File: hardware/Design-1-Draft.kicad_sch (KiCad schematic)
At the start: 37 parts, among them J1 Barrel_Jack_Switch, M1 WATERPUMP-1, M2 WATERPUMP-2, Q1 IRLZ44N, Q2 IRLZ44N, Q3 PN2222A, SW1 Button, U3 ADS1115, U5 Tang_Nano_9K, U7 BOB-12009

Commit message: Updated PCB & SCHEM
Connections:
- net AGND is gone; now on net GND: C7.2
- net GND: now also C8.1, U4.4 (OUT-); no longer C8.2, J1.2
- net at A1.30 (VIN), BZ1.1 (+), C1.1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: now also C8.2, U4.3 (OUT+); no longer C8.1, D1.1 (K)
- net at U4.1 (IN+): now also D1.1 (K)
- net at U4.2 (IN-): now also J1.2
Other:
- moved on the sheet: C8, U4

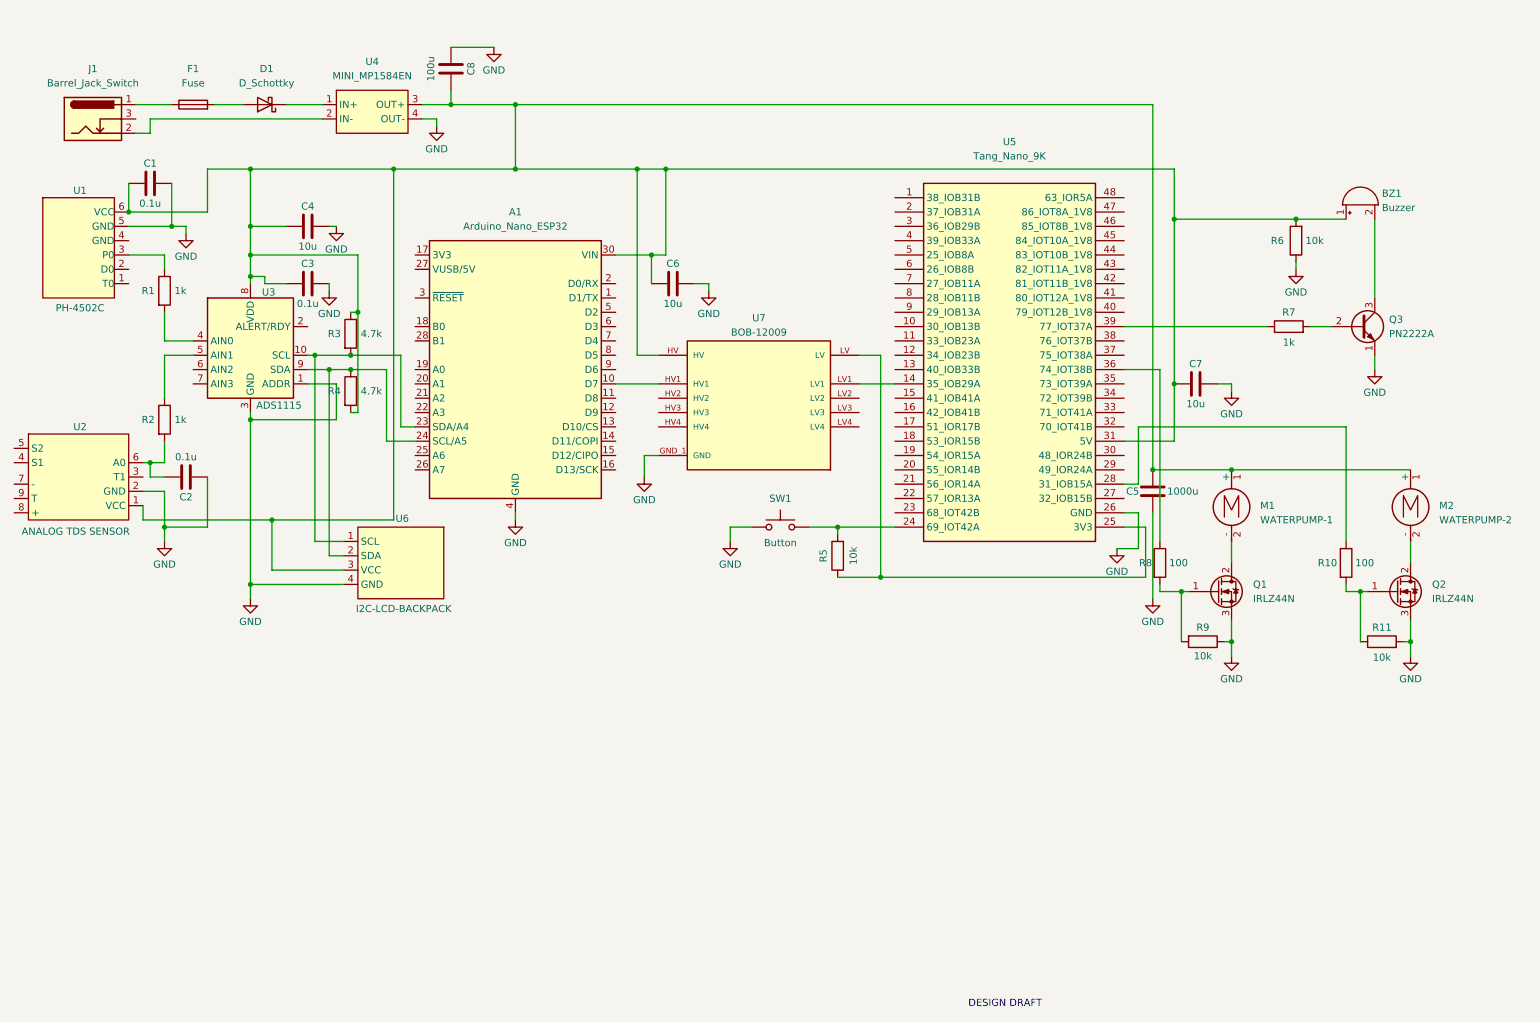
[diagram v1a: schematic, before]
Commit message: updated schem (added multiple caps & 2 flyback diodes @pumps)
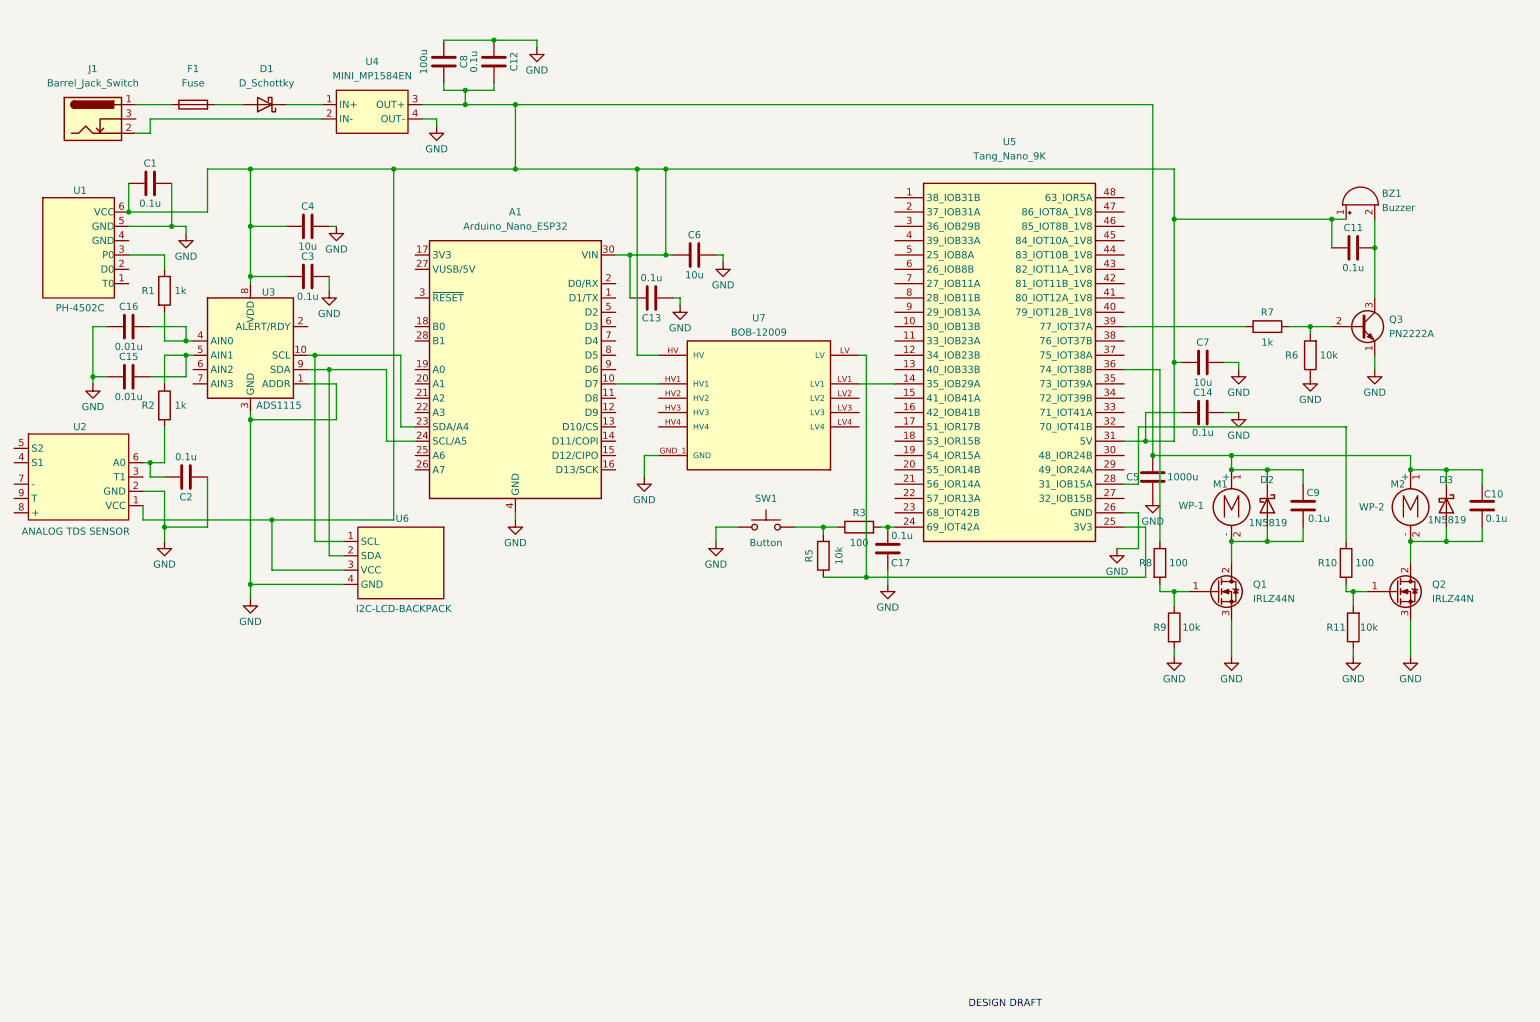
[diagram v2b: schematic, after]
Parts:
- removed R4: 4.7k, Resistor_THT:R_Axial_DIN0207_L6.3mm_D2.5mm_P10.16mm_Horizontal, symbol Device:R
- added C10, C11, C12, C14, C9: 0.1u, Capacitor_THT:C_Radial_D6.3mm_H5.0mm_P2.50mm, symbol Device:C
- added C13, C17: 0.1u, Capacitor_THT:C_Disc_D5.0mm_W2.5mm_P5.00mm, symbol Device:C
- added C15, C16: 0.01u, Capacitor_THT:C_Disc_D5.0mm_W2.5mm_P5.00mm, symbol Device:C
- added D2, D3: 1N5819, Diode_THT:D_DO-41_SOD81_P10.16mm_Horizontal, symbol Diode:1N5819
- M1: value WATERPUMP-1 -> WP-1
- M2: value WATERPUMP-2 -> WP-2
- R3: value 4.7k -> 100
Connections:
- net GND: now also R11.1, R9.2, C12.1, C13.1, C14.2, C15.1, C16.1, C17.2; no longer R11.2, R9.1
- net at Q1.1 (G), R8.2: now also R9.1; no longer R9.2
- net at A1.30 (VIN), BZ1.1 (+), C1.1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: now also C10.1, C11.1, C12.2, C13.2, C14.1, C9.1, D2.1 (K), D3.1 (K); no longer R3.1, R6.2
- net at A1.23 (SDA/A4), U3.10 (SCL), U6.1 (SCL): no longer R3.2
- net at Q3.2 (B), R7.2: now also R6.2
- net at BZ1.2 (-), Q3.3 (C): now also C11.2
- net at R2.1, U3.5 (AIN1): now also C15.2
- net at M1.2 (-), Q1.2 (D): now also C9.2, D2.2 (A)
- net at R5.2, SW1.2: now also R3.1; no longer U5.24 (69_IOT42A)
- net at M2.2 (-), Q2.2 (D): now also C10.2, D3.2 (A)
- net at Q2.1 (G), R10.2: now also R11.2; no longer R11.1
- net at R1.2, U3.4 (AIN0): now also C16.2
- new net: C17.1, R3.2, U5.24 (69_IOT42A)
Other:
- moved on the sheet: C3, C5, C6, C7, C8, R11, R2, R5, R6, R7, R9, SW1

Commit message: Add files via upload
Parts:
- added C18, C19, C21: 0.1u, Capacitor_THT:C_Disc_D5.0mm_W2.5mm_P5.00mm, symbol Device:C
- added C20: 100u, Capacitor_THT:C_Radial_D6.3mm_H5.0mm_P2.50mm, symbol Device:C
- C10, C11, C12, C14, C9: footprint Capacitor_THT:C_Radial_D6.3mm_H5.0mm_P2.50mm -> Capacitor_THT:C_Disc_D5.0mm_W2.5mm_P5.00mm
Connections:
- net GND: now also U4.7 (OUT-), U4.8 (OUT-), C18.1, C19.1, C20.2, C21.2; no longer U4.4 (OUT-)
- net at D1.1 (K), U4.1 (IN+): now also U4.2 (IN+)
- net at A1.30 (VIN), BZ1.1 (+), C1.1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: now also U4.5 (OUT+), C20.1, C21.1; no longer C10.1, C12.2, C5.2, C8.2, C9.1, D2.1 (K), D3.1 (K), M1.1 (+), M2.1 (+), U4.3 (OUT+)
- net at A1.23 (SDA/A4), U3.10 (SCL), U6.1 (SCL): now also C19.2
- net at A1.24 (SCL/A5), U3.9 (SDA), U6.2 (SDA): now also C18.2
- net at J1.2: now also U4.3 (IN-), U4.4 (IN-); no longer U4.2 (IN-)
- new net: C10.1, C12.2, C5.2, C8.2, C9.1, D2.1 (K), D3.1 (K), M1.1 (+), M2.1 (+), U4.6 (OUT+)
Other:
- moved on the sheet: D1, F1

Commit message: Updated PCB and Schem
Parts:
- added C22, C23: 0.1u, Capacitor_THT:C_Disc_D5.0mm_W2.5mm_P5.00mm, symbol Device:C
- added FB1: FerriteBead, Resistor_THT:R_Axial_DIN0207_L6.3mm_D2.5mm_P10.16mm_Horizontal, symbol Device:FerriteBead
- R7: renamed from R8; value 100 -> 150
- R9: renamed from R10; value 100 -> 150
- U7: footprint BOB-12009:CONV_BOB-12009 -> 1_CustomFootprints:CONV_BOB-12009
- renumbered R11 to R10, R5 to R4, R7 to R5, R9 to R8
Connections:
- net GND: now also C3.1, C4.1, J1.2, U4.3 (IN-), U4.4 (IN-), C22.2, C23.2; no longer C3.2, C4.2
- net 5V_ICs: now reaches A1.30 (VIN), BZ1.1 (+), C1.1, C11.1, C13.2, C14.1, C20.1, C21.1, C6.1, C7.1, U1.6 (VCC), U2.1 (VCC), U4.5 (OUT+), U5.31 (5V), U6.3 (VCC), U7.HV
- net 5V_ICs: now also C2.2, C23.1, FB1.1; no longer C3.1, C4.1, U3.8 (VDD)
- net at R2.2, U2.6 (A0): no longer C2.2
- net 5V_PUMPS: now reaches C10.1, C12.2, C5.2, C8.2, C9.1, D2.1 (K), D3.1 (K), M1.1 (+), M2.1 (+), U4.6 (OUT+)
- net +12V: now reaches F1.1, J1.1
- net at U5.14 (35_IOB29A): no longer U7.LV1
- net at R4.1, U5.25 (3V3): no longer U7.LV
- net at U5.28 (31_IOB15A): no longer R9.1
- net at U5.32 (70_IOT41B): now also U7.LV1
- net at U5.35 (73_IOT39A): now also R9.1
- net at A1.17 (3V3): now also U7.LV, C22.1
- new net 5V_ADC: C3.2, C4.2, FB1.2, U3.8 (VDD)
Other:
- moved on the sheet: C2, C3, C4, C6
